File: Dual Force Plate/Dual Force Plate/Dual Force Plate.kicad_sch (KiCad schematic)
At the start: 22 parts, among them J10 Conn_01x07_Pin, J3 Conn_01x07_Pin, J4 Conn_01x07_Pin, J6 Conn_01x02_Pin, J7 Conn_01x04_Pin, J8 Conn_01x02_Pin, J9 Conn_01x07_Pin, SW1 SW_SPST, U1 MT3608, U2 ESP32-DevKitC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

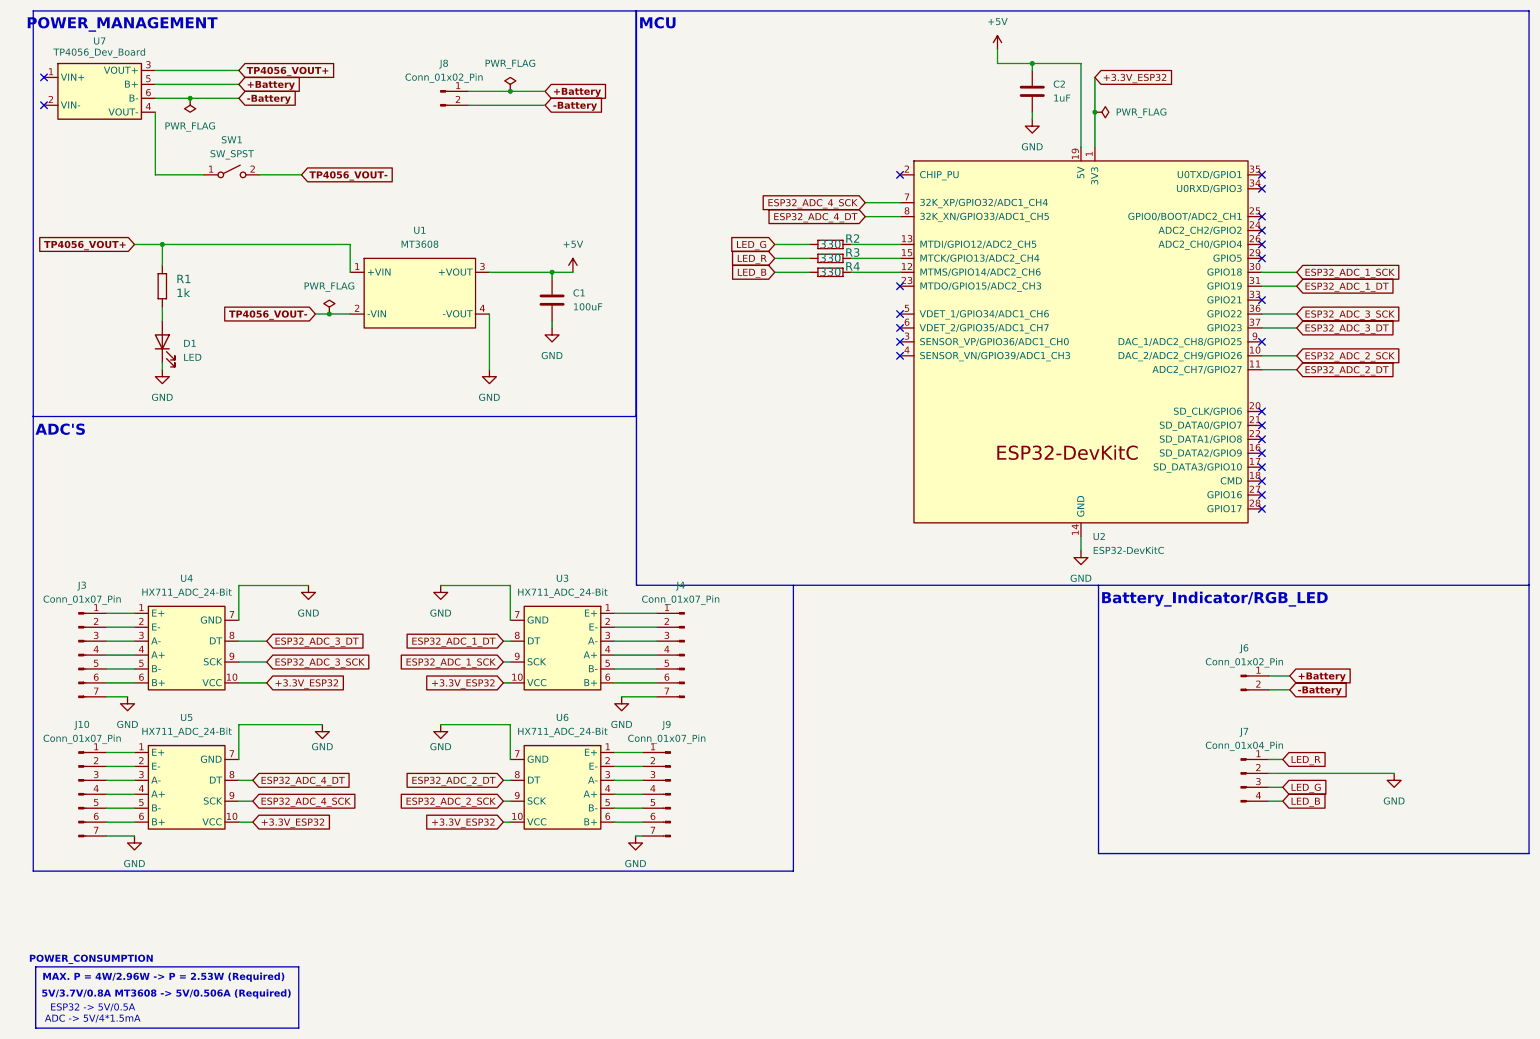
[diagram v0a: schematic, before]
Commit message: Edit the Layout of (DUAL_FORCE_PLATE)
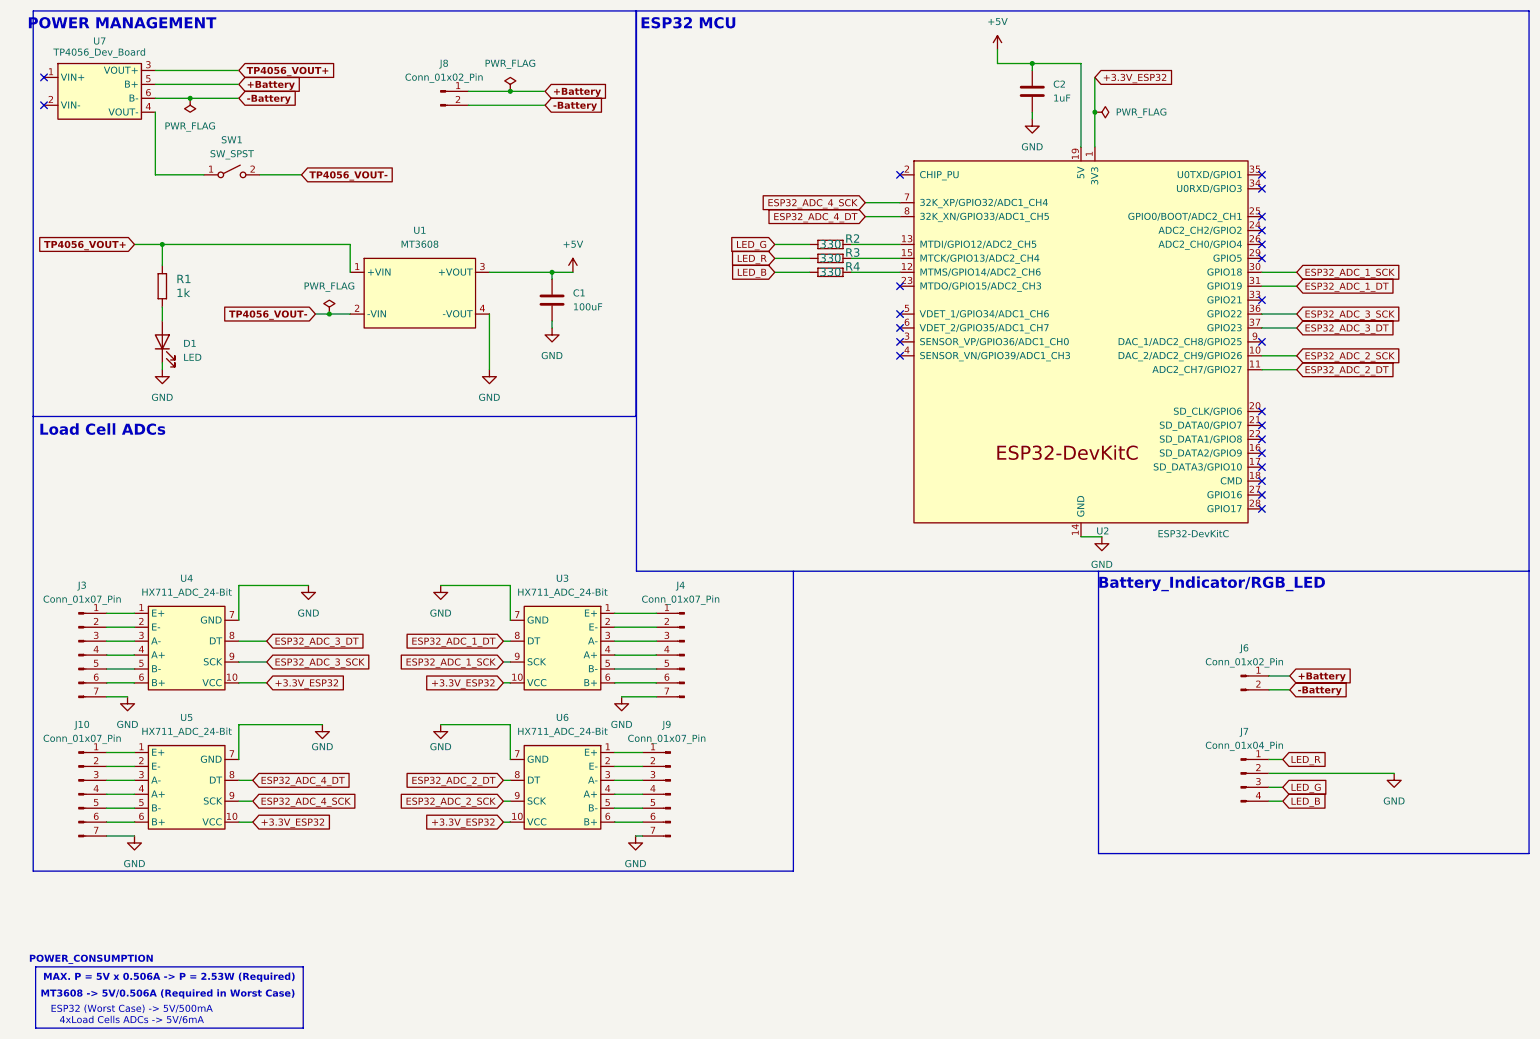
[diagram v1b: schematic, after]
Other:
- note added: "ESP32 (Worst Case) -> 5V/500mA 4xLoad Cells ADCs -> 5V/6mA"
- note added: "ESP32 MCU"
- note added: "Load Cell ADCs"
- note added: "MAX. P = 5V x 0.506A -> P = 2.53W (Required)"
- note added: "MT3608 -> 5V/0.506A (Required in Worst Case)"
- note added: "POWER MANAGEMENT"
- note removed: "5V/3.7V/0.8A MT3608 -> 5V/0.506A (Required)"
- note removed: "ADC'S"
- note removed: "ESP32 -> 5V/0.5A ADC -> 5V/4*1.5mA"
- note removed: "MAX. P = 4W/2.96W -> P = 2.53W (Required)"
- note removed: "MCU"
- note removed: "POWER_MANAGEMENT"
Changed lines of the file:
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@@
 	(rectangle
 		(start 122.08 12)
-		(end 284.96 116.8)
+		(end 284.96 114.24)
 		(stroke
 			(width 0)
@@
 	(rectangle
 		(start 12.446 186.436)
-		(end 60.452 197.612)
+		(end 61.28 197.612)
 		(stroke
 			(width 0)
@@
 		)
 	)
-	(text "5V/3.7V/0.8A MT3608 -> 5V/0.506A (Required)"
+	(text "MT3608 -> 5V/0.506A (Required in Worst Case)"
 		(exclude_from_sim no)
-		(at 36.322 191.516 0)
+		(at 36.576 191.516 0)
 		(effects
 			(font
@@
 		)
 	)
-	(text "ESP32 -> 5V/0.5A\nADC -> 5V/4*1.5mA\n"
+	(text "ESP32 (Worst Case) -> 5V/500mA\n4xLoad Cells ADCs -> 5V/6mA\n"
 		(exclude_from_sim no)
-		(at 22.86 195.072 0)
+		(at 29.972 195.326 0)
 		(effects
 			(font
@@
 		)
 	)
-	(text "ADC'S"
+	(text "Load Cell ADCs"
 		(exclude_from_sim no)
-		(at 17.018 88.646 0)
+		(at 24.638 88.646 0)
 		(effects
 			(font
@@
 		)
 	)
-	(text "MCU"
+	(text "ESP32 MCU"
 		(exclude_from_sim no)
-		(at 125.984 14.478 0)
+		(at 131.572 14.478 0)
 		(effects
 			(font
@@
 	(text "Battery_Indicator/RGB_LED"
 		(exclude_from_sim no)
-		(at 227.584 119.38 0)
+		(at 227.076 116.586 0)
 		(effects
 			(font
@@
 		)
 	)
-	(text "MAX. P = 4W/2.96W -> P = 2.53W (Required)"
+	(text "MAX. P = 5V x 0.506A -> P = 2.53W (Required)"
 		(exclude_from_sim no)
-		(at 35.814 188.468 0)
+		(at 36.83 188.468 0)
 		(effects
 			(font
@@
 		)
 	)
-	(text "POWER_MANAGEMENT"
+	(text "POWER MANAGEMENT"
 		(exclude_from_sim no)
 		(at 28.194 14.478 0)
@@
 	(polyline
 		(pts
-			(xy 150.72 116.8) (xy 150.72 168.96)
+			(xy 150.72 114.24) (xy 150.72 168.96)
 		)
 		(stroke
@@
 	(wire
 		(pts
+			(xy 207.01 107.95) (xy 203.2 107.95)
+		)
+		(stroke
+			(width 0)
+			(type default)
+		)
+	)
+	(wire
+		(pts
 			(xy 49.53 116.84) (xy 62.23 116.84)
 		)
@@
 	(wire
 		(pts
-			(xy 203.2 110.49) (xy 203.2 107.95)
-		)
-		(stroke
-			(width 0)
-			(type default)
-		)
-	)
-	(wire
-		(pts
 			(xy 25.4 121.92) (xy 30.48 121.92)
 		)
@@
 	(polyline
 		(pts
-			(xy 206.4 116.8) (xy 206.4 165.76)
+			(xy 206.4 114.24) (xy 206.4 165.76)
 		)
 		(stroke
@@
 	(polyline
 		(pts
-			(xy 284.96 116.8) (xy 284.96 165.76)
+			(xy 284.96 114.24) (xy 284.96 165.76)
 		)
 		(stroke
@@
 	(symbol
 		(lib_id "power:GND")
-		(at 203.2 110.49 0)
+		(at 207.01 107.95 0)
 		(unit 1)
 		(body_style 1)
@@
 		(fields_autoplaced yes)
 		(property "Reference" "#PWR07"
-			(at 203.2 116.84 0)
+			(at 207.01 114.3 0)
 			(hide yes)
 			(show_name no)
@@
 		)
 		(property "Value" "GND"
-			(at 203.2 115.57 0)
+			(at 207.01 113.03 0)
 			(show_name no)
 			(do_not_autoplace no)
@@
 		)
 		(property "Footprint" ""
-			(at 203.2 110.49 0)
+			(at 207.01 107.95 0)
 			(hide yes)
 			(show_name no)
@@
 		)
 		(property "Datasheet" ""
-			(at 203.2 110.49 0)
+			(at 207.01 107.95 0)
 			(hide yes)
 			(show_name no)
@@
 		)
 		(property "Description" "Power symbol creates a global label with name \"GND\" , ground"
-			(at 203.2 110.49 0)
+			(at 207.01 107.95 0)
 			(hide yes)
 			(show_name no)
@@
 		(in_pos_files yes)
 		(dnp no)
-		(fields_autoplaced yes)
 		(property "Reference" "U2"
-			(at 205.3433 107.95 0)
+			(at 205.994 106.934 0)
 			(show_name no)
 			(do_not_autoplace no)
@@
 		)
 		(property "Value" "ESP32-DevKitC"
-			(at 205.3433 110.49 0)
+			(at 217.17 107.442 0)
 			(show_name no)
 			(do_not_autoplace no)
